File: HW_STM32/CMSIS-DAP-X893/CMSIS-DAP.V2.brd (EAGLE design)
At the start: 31.2 x 13.6 mm, 35 parts, among them IC1 STM32F103CBT6, J3 USB-4-A-SMD, Q1 8M, U7 TPS73033, X1 USB-SMD

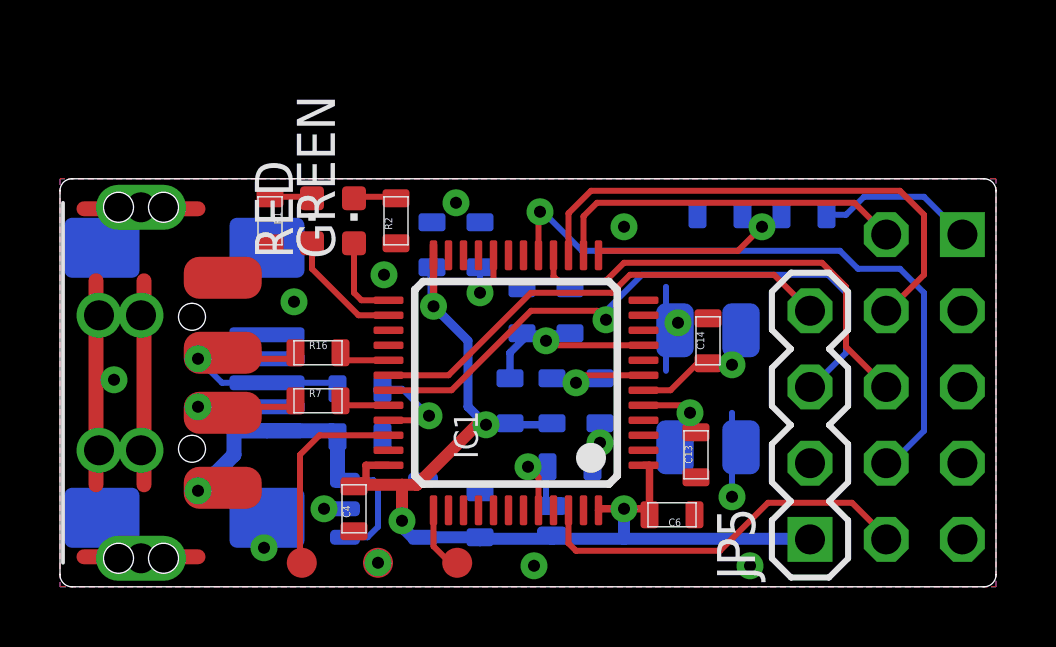
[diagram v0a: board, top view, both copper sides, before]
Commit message: Fix RESET pin
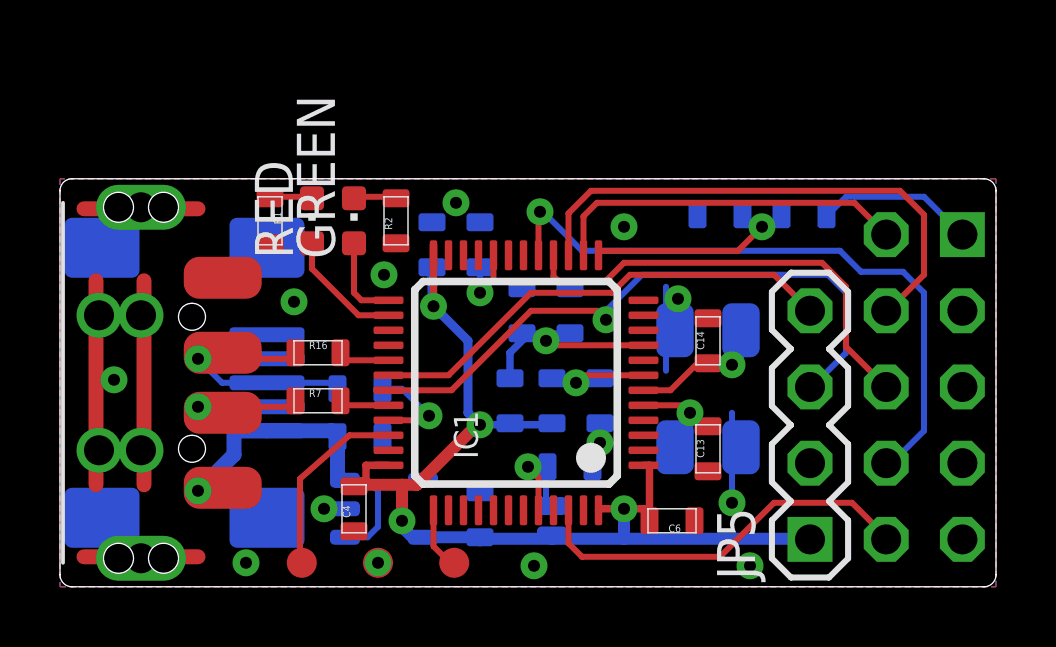
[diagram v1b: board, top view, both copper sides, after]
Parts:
- C13, C14: value 20p -> 15p
- IC1: value STM32F103CBT6 -> STM32F102C8-B/STM32F103C8-B
- moved C13 0.45 mm to (21.6, 4.60)
- moved C6 0.20 mm to (20.4, 2.20)
- moved SWCLK 0.10 mm to (13.1, 0.80)
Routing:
- net PA13-SWDIO: track 6.88 -> 6.36 mm
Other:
- board text added: "Version 2"

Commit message: Add HEX file
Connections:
- net PA10 renamed PA10-RX
- net PA9 renamed PA9-TX
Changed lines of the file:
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@@
 <?xml version="1.0" encoding="utf-8"?>
 <!DOCTYPE eagle SYSTEM "eagle.dtd">
-<eagle version="6.4">
+<eagle version="7.1.0">
 <drawing>
 <settings>
@@
 <pass name="Default">
 <param name="RoutingGrid" value="50mil"/>
+<param name="AutoGrid" value="1"/>
+<param name="Efforts" value="0"/>
+<param name="TopRouterVariant" value="1"/>
 <param name="tpViaShape" value="round"/>
 <param name="PrefDir.1" value="|"/>
@@
 <wire x1="15.75" y1="8.4" x2="15.4" y2="8.45" width="0.25" layer="16"/>
 </signal>
-<signal name="PA9">
+<signal name="PA9-TX">
 <contactref element="IC1" pad="30"/>
 <wire x1="10.95" y1="7.05" x2="12.95" y2="7.05" width="0.2" layer="1"/>
@@
 <wire x1="11.15" y1="13" x2="11.2" y2="12.95" width="0.2" layer="1"/>
 </signal>
-<signal name="PA10">
+<signal name="PA10-RX">
 <contactref element="IC1" pad="31"/>
 <wire x1="10.95" y1="6.55" x2="13.05" y2="6.55" width="0.2" layer="1"/>
